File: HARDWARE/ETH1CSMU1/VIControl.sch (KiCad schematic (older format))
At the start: 102 parts

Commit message: Added ADC
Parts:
- added C406, C407, C408, C409, C410, C411, C412, C413, C414, C415, C416, C417, C418, C419, C420, C421, C422, C423: 100n, symbol Device:C
- D411, D412: renamed from D?; footprint Package_TO_SOT_SMD:SOT-23 -> (none)
- U402, U409: renamed from U?; footprint Package_SO:SOIC-8_3.9x4.9mm_P1.27mm -> (none)
- gave numbers to parts that had none: 78
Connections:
- net +15V: now also U401.8 (V+), U411.8 (V+), U412.8 (V+), U413.8 (V+), U415.8 (V+), U418.8 (V+), C407.1, C409.1, C411.1, C413.1, C415.1, C417.1, C419.1, C421.1, C423.1; no longer U401.8 (V+), U401.8 (V+), U403.8 (V+), U403.8 (V+), U407.8 (V+), U407.8 (V+)
- net +5V: now also U410.5 (VEE), U410.6 (GND); no longer U410.10 (VCC), U410.9 (VS)
- net +IDAC: now also U412.5 (+); no longer U412.5 (+)
- net -15V: now also U401.4 (V-), U411.4 (V-), U412.4 (V-), U413.4 (V-), U415.4 (V-), U418.4 (V-), C406.1, C408.1, C410.1, C412.1, C414.1, C416.1, C418.1, C420.1, C422.1; no longer U401.4 (V-), U401.4 (V-), U403.4 (V-), U403.4 (V-), U407.4 (V-), U407.4 (V-)
- net -IDAC: now also U412.3 (+); no longer U412.3 (+)
- net CurrentBoostIN: now also U415.7; no longer U415.7
- net GND: now also U401.3 (+), U410.10 (VCC), U410.9 (VS), U411.3 (+), U415.3 (+), U415.5 (+), C406.2, C407.2, C408.2, C409.2, C410.2, C411.2, C412.2, C413.2, C414.2, C415.2, C416.2, C417.2, C418.2, C419.2, C420.2, C421.2, C422.2, C423.2; no longer U401.3 (+), U410.5 (VEE), U410.6 (GND), U411.3 (+), U415.3 (+), U415.5 (+)
- net VI_CLAMP: now also U407.6 (-), U407.7; no longer U415.6 (-), U415.7
- net at U406.11 (VOUTB): now also U401.5 (+); no longer U411.5 (+)
- net at U406.5 (VOUTC): now also U411.5 (+); no longer U411.5 (+)
- net at R411.1, R415.2: now also U411.1; no longer U401.1
- net at R408.1, R411.2: now also U411.2 (-); no longer U401.2 (-)
- net at R412.1, R416.2: now also U411.7; no longer U411.7
- net at R406.1, R412.2: now also U411.6 (-); no longer U411.6 (-)
- net at R413.1, R417.2: now also U401.1; no longer U411.1
- net at R409.1, R413.2: now also U401.2 (-); no longer U411.2 (-)
- net at R414.1, R418.2: now also U401.7; no longer U411.7
- net at R407.1, R414.2: now also U401.6 (-); no longer U411.6 (-)
- net at D403.2 (A), R421.2: now also U412.2 (-); no longer U412.2 (-)
- net at D403.1 (K), D407.2 (A): now also U412.1; no longer U412.1
- net at D404.1 (K), R422.2: now also U412.6 (-); no longer U412.6 (-)
- net at D404.2 (A), D408.1 (K): now also U412.7; no longer U412.7
- net at D409.1 (K), D410.2 (A), R426.1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: now also U407.5 (+); no longer U415.5 (+)
- net at C404.1, D401.2 (A), D402.1 (K)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: now also U407.2 (-); no longer U412.2 (-)
- net at C404.2, D401.1 (K), D402.2 (A)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: now also U407.1; no longer U412.1
- net at R410.1: now also U407.3 (+); no longer U412.3 (+)
- net at C405.2, R428.1, R431.2: now also U415.2 (-); no longer U415.2 (-)
- net at C405.1, R431.1, R434.2: now also U415.1; no longer U415.1
- net at R434.1, R435.2: now also U415.6 (-); no longer U415.6 (-)
- net at R436.2, U418.1: now also U410.3 (-); no longer U410.2 (-)
- net at R446.2, R447.2: now also U403.3 (+); no longer U418.5 (+)
- net at R438.1, R445.2: now also U403.2 (-); no longer U418.6 (-)
- net at R437.1, R442.2: now also U418.6 (-); no longer U418.2 (-)
- net at R443.2, R444.2: now also U418.5 (+); no longer U418.3 (+)
- net at R419.2, R420.1: now also U403.5 (+); no longer U413.5 (+)
- net at D412.1: now also U410.7; no longer U410.8
- net at D412.2: now also U410.8; no longer U410.7
- new net: R438.2, U403.1, U410.1 (+)
- new net: U403.6 (-), U403.7
- new net: R437.2, U410.2 (-), U410.4 (+), U418.7
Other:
- moved on the sheet: C405, R419, R420, R428, R431, R432, R434, R435, U403C, U407C, U409B, U412A

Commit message: Commit
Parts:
- C406, C407, C408, C409, C410, C411, C412, C413, C414, C415, C416, C417, C418, C419, C420, C421, C422, C423: footprint (none) -> SMD:C_0603_Symbol1
- R406, R407, R408, R409, R410, R415, R416, R417, R418, R419, R420, R421, R422, R423, R424, R425, R428, R431, R433, R434, R435, R439, R440, R442, R443, R445, R446: footprint (none) -> SMD:R_0603_Symbol1
- R429, R430, R432: footprint (none) -> SMD:R_0603_Symbol2
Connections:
- net VREF renamed VREF+2V5
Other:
- moved on the sheet: D411, D412, R427, R429, R430, R433, R436, R437, R438, R439, R440, R441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

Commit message: Footprints
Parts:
- removed R432: 0, SMD:R_0603_Symbol2, symbol Device:R
- added C405, C406, C407, C408, C409, C410, C411, C412, C413, C414, C415, C435, C436: 100n, SMD:C_0603_Symbol1, symbol Device:C
- added U416: DG419xY, symbol Analog_Switch:DG419xY
- added U418: SN74LVC1T45, symbol logic_local:SN74LVC1T45
- C420: renamed from C405; footprint (none) -> SMD:C_0603_Symbol5
- D401, D402, D403, D404, D405, D406, D407, D408, D409, D410: value D_Schottky -> BAT54-02V
- renumbered C406 to C416, C407 to C417, C408 to C418, C409 to C419, C410 to C421, C411 to C422, C412 to C423, C413 to C424, C414 to C425, C415 to C426, C416 to C427, C417 to C428, C418 to C429, C419 to C430, C420 to C431, C421 to C432, C422 to C433, C423 to C434, R419 to R415, R420 to R416, R415 to R417, R416 to R418, R417 to R419, R418 to R420, R429 to R428, R428 to R429, R433 to R432, R434 to R433, R435 to R434, R436 to R435, R437 to R436, R438 to R437, R439 to R438, R440 to R439, R441 to R440, R442 to R441, R443 to R442, R444 to R443, R445 to R444, R446 to R445, R447 to R446, U411 to U402, U402 to U403, U418 to U404, U404 to U405, U405 to U406, U413 to U407, U403 to U408, U406 to U409, U415 to U410, U412 to U411, U408 to U412, U407 to U413, U409 to U414, U410 to U415, U414 to U417, U416 to U419, U417 to U420
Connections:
- net +15V: now also C436.1, U416.5 (VL)
- net +3V3: now also C406.1, C408.1, C410.1, C412.1, C414.1, U418.1 (VCCA)
- net +5V: now also C405.1, C407.1, C409.1, C411.1, C413.1, C415.1, U416.4 (V+), U418.6 (VCCB)
- net -15V: now also C435.1, U416.3 (GND)
- net CurrentBoostIN: now also U416.1; no longer R434.1, U410.7
- net GND: now also C405.2, C406.2, C407.2, C408.2, C409.2, C410.2, C411.2, C412.2, C413.2, C414.2, C415.2, C435.2, C436.2, U416.7 (V-), U418.2 (GND), U418.5 (DIR)
- net SIGN_SELECT: now also U418.3 (A)
- net VI_CLAMP: now also U416.8
- new net: R434.1, U410.7, U416.2
- new net: U416.6, U418.4 (B)
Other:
- moved on the sheet: C416, C417, C418, C419, C421, C422, C423, C424, C425, C426, C427, C428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

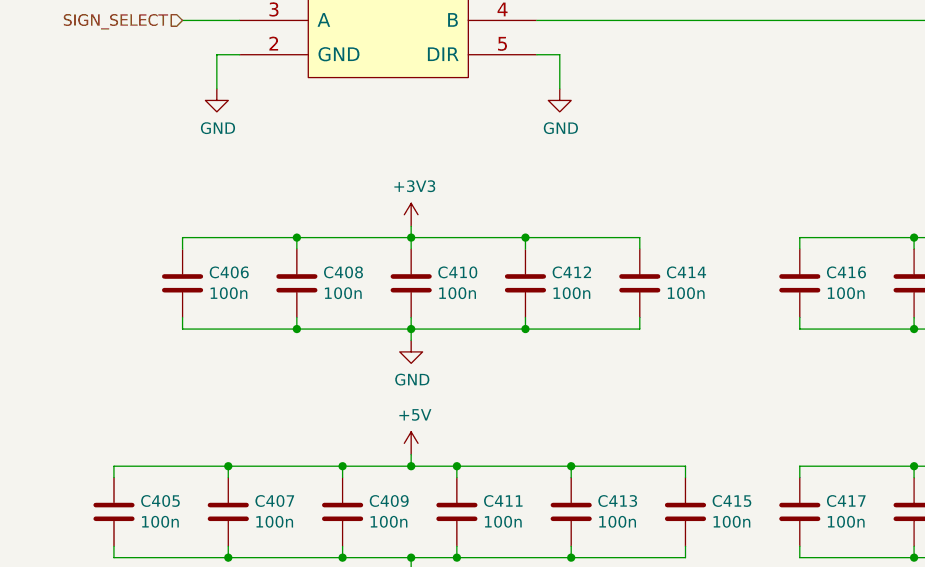
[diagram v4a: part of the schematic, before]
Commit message: Footprint selection
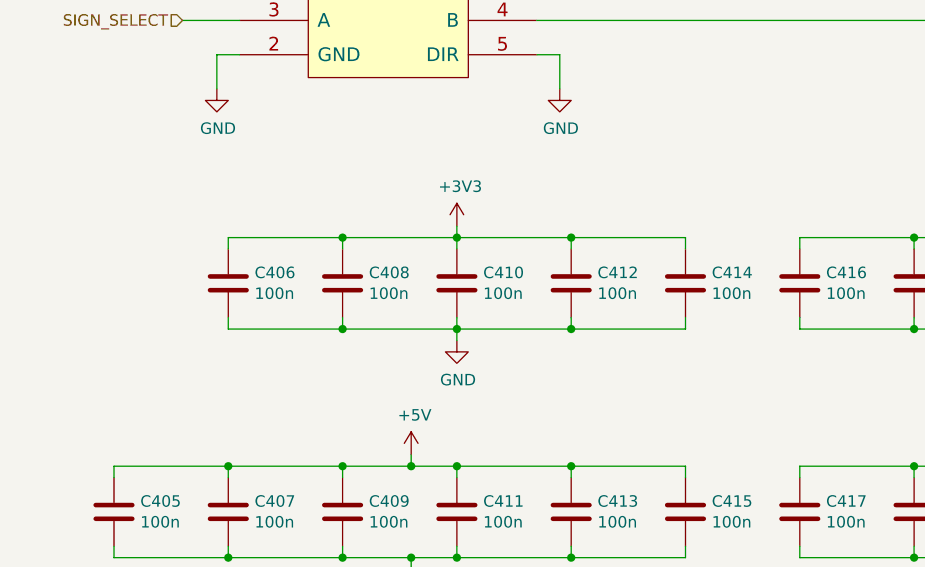
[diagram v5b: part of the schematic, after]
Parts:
- D401, D402, D403, D404, D405, D406, D407, D408, D409, D410: footprint (none) -> Diodes_SMD:D_SOD-523
- R401, R402: footprint (none) -> SMD:R_0603_Symbol2
- R403, R404: footprint (none) -> Resistors_SMD:R_0603
- R412, R414: footprint (none) -> SMD:R_0603_Symbol7
- R435, R436, R437, R440, R443, R446: footprint (none) -> SMD:R_0603_Symbol5
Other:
- moved on the sheet: C406, C408, C410, C412, C414
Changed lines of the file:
@@
 F 0 "R412" V 5493 2350 50  0000 C CNN
 F 1 "30k" V 5584 2350 50  0000 C CNN
-F 2 "" V 5630 2350 50  0001 C CNN
+F 2 "SMD:R_0603_Symbol7" V 5630 2350 50  0001 C CNN
 F 3 "~" H 5700 2350 50  0001 C CNN
 	1    5700 2350
@@
 F 0 "R414" V 5493 4800 50  0000 C CNN
 F 1 "30k" V 5584 4800 50  0000 C CNN
-F 2 "" V 5630 4800 50  0001 C CNN
+F 2 "SMD:R_0603_Symbol7" V 5630 4800 50  0001 C CNN
 F 3 "~" H 5700 4800 50  0001 C CNN
 	1    5700 4800
@@
 F 0 "D403" V 8146 1221 50  0000 R CNN
 F 1 "BAT54-02V" V 8055 1221 50  0000 R CNN
-F 2 "" H 8100 1300 50  0001 C CNN
+F 2 "Diodes_SMD:D_SOD-523" H 8100 1300 50  0001 C CNN
 F 3 "~" H 8100 1300 50  0001 C CNN
 	1    8100 1300
@@
 F 0 "D407" H 8300 1600 50  0000 C CNN
 F 1 "BAT54-02V" H 8300 1700 50  0000 C CNN
-F 2 "" H 8300 1500 50  0001 C CNN
+F 2 "Diodes_SMD:D_SOD-523" H 8300 1500 50  0001 C CNN
 F 3 "~" H 8300 1500 50  0001 C CNN
 	1    8300 1500
@@
 F 0 "D404" V 8054 2629 50  0000 L CNN
 F 1 "BAT54-02V" V 8145 2629 50  0000 L CNN
-F 2 "" H 8100 2550 50  0001 C CNN
+F 2 "Diodes_SMD:D_SOD-523" H 8100 2550 50  0001 C CNN
 F 3 "~" H 8100 2550 50  0001 C CNN
 	1    8100 2550
@@
 F 0 "D408" H 8300 2650 50  0000 C CNN
 F 1 "BAT54-02V" H 8300 2550 50  0000 C CNN
-F 2 "" H 8300 2750 50  0001 C CNN
+F 2 "Diodes_SMD:D_SOD-523" H 8300 2750 50  0001 C CNN
 F 3 "~" H 8300 2750 50  0001 C CNN
 	1    8300 2750
@@
 F 0 "D405" V 8146 3671 50  0000 R CNN
 F 1 "BAT54-02V" V 8055 3671 50  0000 R CNN
-F 2 "" H 8100 3750 50  0001 C CNN
+F 2 "Diodes_SMD:D_SOD-523" H 8100 3750 50  0001 C CNN
 F 3 "~" H 8100 3750 50  0001 C CNN
 	1    8100 3750
@@
 F 0 "D409" H 8300 4050 50  0000 C CNN
 F 1 "BAT54-02V" H 8300 4150 50  0000 C CNN
-F 2 "" H 8300 3950 50  0001 C CNN
+F 2 "Diodes_SMD:D_SOD-523" H 8300 3950 50  0001 C CNN
 F 3 "~" H 8300 3950 50  0001 C CNN
 	1    8300 3950
@@
 F 0 "D406" V 8054 5079 50  0000 L CNN
 F 1 "BAT54-02V" V 8145 5079 50  0000 L CNN
-F 2 "" H 8100 5000 50  0001 C CNN
+F 2 "Diodes_SMD:D_SOD-523" H 8100 5000 50  0001 C CNN
 F 3 "~" H 8100 5000 50  0001 C CNN
 	1    8100 5000
@@
 F 0 "D410" H 8300 5100 50  0000 C CNN
 F 1 "BAT54-02V" H 8300 5000 50  0000 C CNN
-F 2 "" H 8300 5200 50  0001 C CNN
+F 2 "Diodes_SMD:D_SOD-523" H 8300 5200 50  0001 C CNN
 F 3 "~" H 8300 5200 50  0001 C CNN
 	1    8300 5200
@@
 F 0 "D401" V 7346 6271 50  0000 R CNN
 F 1 "BAT54-02V" V 7255 6271 50  0000 R CNN
-F 2 "" H 7300 6350 50  0001 C CNN
+F 2 "Diodes_SMD:D_SOD-523" H 7300 6350 50  0001 C CNN
 F 3 "~" H 7300 6350 50  0001 C CNN
 	1    7300 6350
@@
 F 0 "D402" V 7854 6429 50  0000 L CNN
 F 1 "BAT54-02V" V 7945 6429 50  0000 L CNN
-F 2 "" H 7900 6350 50  0001 C CNN
+F 2 "Diodes_SMD:D_SOD-523" H 7900 6350 50  0001 C CNN
 F 3 "~" H 7900 6350 50  0001 C CNN
 	1    7900 6350
@@
 F 0 "R404" H 3620 7746 50  0000 L CNN
 F 1 "75k" H 3620 7655 50  0000 L CNN
-F 2 "" V 3480 7700 50  0001 C CNN
+F 2 "Resistors_SMD:R_0603" V 3480 7700 50  0001 C CNN
 F 3 "~" H 3550 7700 50  0001 C CNN
 	1    3550 7700
@@
 F 0 "R403" V 3093 7500 50  0000 C CNN
 F 1 "12k4" V 3184 7500 50  0000 C CNN
-F 2 "" V 3230 7500 50  0001 C CNN
+F 2 "Resistors_SMD:R_0603" V 3230 7500 50  0001 C CNN
 F 3 "~" H 3300 7500 50  0001 C CNN
 	1    3300 7500
@@
 F 0 "R402" H 2480 3904 50  0000 R CNN
 F 1 "0" H 2480 3995 50  0000 R CNN
-F 2 "" V 2480 3950 50  0001 C CNN
+F 2 "SMD:R_0603_Symbol2" V 2480 3950 50  0001 C CNN
 F 3 "~" H 2550 3950 50  0001 C CNN
 	1    2550 3950
@@
 F 0 "R401" H 2130 3904 50  0000 R CNN
 F 1 "0" H 2130 3995 50  0000 R CNN
-F 2 "" V 2130 3950 50  0001 C CNN
+F 2 "SMD:R_0603_Symbol2" V 2130 3950 50  0001 C CNN
 F 3 "~" H 2200 3950 50  0001 C CNN
 	1    2200 3950
@@
 F 0 "R435" V 14343 800 50  0000 C CNN
 F 1 "2k49" V 14434 800 50  0000 C CNN
-F 2 "" V 14480 800 50  0001 C CNN
+F 2 "SMD:R_0603_Symbol5" V 14480 800 50  0001 C CNN
 F 3 "~" H 14550 800 50  0001 C CNN
 	1    14550 800
@@
 F 0 "R440" V 14993 1700 50  0000 C CNN
 F 1 "2k49" V 15084 1700 50  0000 C CNN
-F 2 "" V 15130 1700 50  0001 C CNN
+F 2 "SMD:R_0603_Symbol5" V 15130 1700 50  0001 C CNN
 F 3 "~" H 15200 1700 50  0001 C CNN
 	1    15200 1700
@@
 F 0 "R437" V 14343 3500 50  0000 C CNN
 F 1 "2k49" V 14434 3500 50  0000 C CNN
-F 2 "" V 14480 3500 50  0001 C CNN
+F 2 "SMD:R_0603_Symbol5" V 14480 3500 50  0001 C CNN
 F 3 "~" H 14550 3500 50  0001 C CNN
 	1    14550 3500
@@
 F 0 "R446" V 14993 4400 50  0000 C CNN
 F 1 "2k49" V 15084 4400 50  0000 C CNN
-F 2 "" V 15130 4400 50  0001 C CNN
+F 2 "SMD:R_0603_Symbol5" V 15130 4400 50  0001 C CNN
 F 3 "~" H 15200 4400 50  0001 C CNN
 	1    15200 4400
@@
 F 0 "R436" V 14343 2150 50  0000 C CNN
 F 1 "2k49" V 14434 2150 50  0000 C CNN
-F 2 "" V 14480 2150 50  0001 C CNN
+F 2 "SMD:R_0603_Symbol5" V 14480 2150 50  0001 C CNN
 F 3 "~" H 14550 2150 50  0001 C CNN
 	1    14550 2150
@@
 F 0 "R443" V 14993 3050 50  0000 C CNN
 F 1 "2k49" V 15084 3050 50  0000 C CNN
-F 2 "" V 15130 3050 50  0001 C CNN
+F 2 "SMD:R_0603_Symbol5" V 15130 3050 50  0001 C CNN
 F 3 "~" H 15200 3050 50  0001 C CNN
 	1    15200 3050
@@
 L Device:C C406
 U 1 1 5C341DFF
-P 8400 8450
-F 0 "C406" H 8515 8496 50  0000 L CNN
-F 1 "100n" H 8515 8405 50  0000 L CNN
-F 2 "SMD:C_0603_Symbol1" H 8438 8300 50  0001 C CNN
-F 3 "~" H 8400 8450 50  0001 C CNN
-	1    8400 8450
+P 8600 8450
+F 0 "C406" H 8715 8496 50  0000 L CNN
+F 1 "100n" H 8715 8405 50  0000 L CNN
+F 2 "SMD:C_0603_Symbol1" H 8638 8300 50  0001 C CNN
+F 3 "~" H 8600 8450 50  0001 C CNN
+	1    8600 8450
 	1    0    0    -1
 $EndComp
@@
 L Device:C C408
 U 1 1 5C341E05
-P 8900 8450
-F 0 "C408" H 9015 8496 50  0000 L CNN
-F 1 "100n" H 9015 8405 50  0000 L CNN
-F 2 "SMD:C_0603_Symbol1" H 8938 8300 50  0001 C CNN
-F 3 "~" H 8900 8450 50  0001 C CNN
-	1    8900 8450
+P 9100 8450
+F 0 "C408" H 9215 8496 50  0000 L CNN
+F 1 "100n" H 9215 8405 50  0000 L CNN
+F 2 "SMD:C_0603_Symbol1" H 9138 8300 50  0001 C CNN
+F 3 "~" H 9100 8450 50  0001 C CNN
+	1    9100 8450
 	1    0    0    -1
 $EndComp
@@
 L Device:C C410
 U 1 1 5C341E0B
-P 9400 8450
-F 0 "C410" H 9515 8496 50  0000 L CNN
-F 1 "100n" H 9515 8405 50  0000 L CNN
-F 2 "SMD:C_0603_Symbol1" H 9438 8300 50  0001 C CNN
-F 3 "~" H 9400 8450 50  0001 C CNN
-	1    9400 8450
+P 9600 8450
+F 0 "C410" H 9715 8496 50  0000 L CNN
+F 1 "100n" H 9715 8405 50  0000 L CNN
+F 2 "SMD:C_0603_Symbol1" H 9638 8300 50  0001 C CNN
+F 3 "~" H 9600 8450 50  0001 C CNN
+	1    9600 8450
 	1    0    0    -1
 $EndComp
@@
 L Device:C C412
 U 1 1 5C341E11
-P 9900 8450
-F 0 "C412" H 10015 8496 50  0000 L CNN
-F 1 "100n" H 10015 8405 50  0000 L CNN
-F 2 "SMD:C_0603_Symbol1" H 9938 8300 50  0001 C CNN
-F 3 "~" H 9900 8450 50  0001 C CNN
-	1    9900 8450
+P 10100 8450
+F 0 "C412" H 10215 8496 50  0000 L CNN
+F 1 "100n" H 10215 8405 50  0000 L CNN
+F 2 "SMD:C_0603_Symbol1" H 10138 8300 50  0001 C CNN
+F 3 "~" H 10100 8450 50  0001 C CNN
+	1    10100 8450
 	1    0    0    -1
 $EndComp
@@
 L Device:C C414
 U 1 1 5C341E17
-P 10400 8450
-F 0 "C414" H 10515 8496 50  0000 L CNN
-F 1 "100n" H 10515 8405 50  0000 L CNN
-F 2 "SMD:C_0603_Symbol1" H 10438 8300 50  0001 C CNN
-F 3 "~" H 10400 8450 50  0001 C CNN
-	1    10400 8450
+P 10600 8450
+F 0 "C414" H 10715 8496 50  0000 L CNN
+F 1 "100n" H 10715 8405 50  0000 L CNN
+F 2 "SMD:C_0603_Symbol1" H 10638 8300 50  0001 C CNN
+F 3 "~" H 10600 8450 50  0001 C CNN
+	1    10600 8450
 	1    0    0    -1
 $EndComp
 Wire Wire Line
-	8400 8300 8400 8250
+	8600 8300 8600 8250
 Wire Wire Line
-	8400 8250 8900 8250
+	8600 8250 9100 8250
 Wire Wire Line
-	10400 8300 10400 8250
+	10600 8300 10600 8250
 Wire Wire Line
-	9900 8300 9900 8250
-Connection ~ 9900 8250
+	10100 8300 10100 8250
+Connection ~ 10100 8250
 Wire Wire Line
-	9900 8250 10400 8250
+	10100 8250 10600 8250
 Wire Wire Line
-	9400 8300 9400 8250
-Connection ~ 9400 8250
+	9600 8300 9600 8250
+Connection ~ 9600 8250
 Wire Wire Line
-	9400 8250 9900 8250
+	9600 8250 10100 8250
 Wire Wire Line
-	8900 8300 8900 8250
-Connection ~ 8900 8250
+	9100 8300 9100 8250
+Connection ~ 9100 8250
 Wire Wire Line
-	8900 8250 9400 8250
+	9100 8250 9600 8250
 Wire Wire Line
-	8400 8600 8400 8650
+	8600 8600 8600 8650
 Wire Wire Line
-	8400 8650 8900 8650
+	8600 8650 9100 8650
 Wire Wire Line
-	10400 8600 10400 8650
+	10600 8600 10600 8650
 Wire Wire Line
-	9900 8600 9900 8650
-Connection ~ 9900 8650
+	10100 8600 10100 8650
+Connection ~ 10100 8650
 Wire Wire Line
-	9900 8650 10400 8650
+	10100 8650 10600 8650
 Wire Wire Line
-	9400 8600 9400 8650
-Connection ~ 9400 8650
+	9600 8600 9600 8650
+Connection ~ 9600 8650
 Wire Wire Line
-	9400 8650 9900 8650
+	9600 8650 10100 8650
 Wire Wire Line
-	8900 8600 8900 8650
-Connection ~ 8900 8650
+	9100 8600 9100 8650
+Connection ~ 9100 8650
 Wire Wire Line
-	8900 8650 9400 8650
+	9100 8650 9600 8650
 $Comp
 L power:GND #PWR0461
 U 1 1 5C49DEA2
-P 9400 8700
-F 0 "#PWR0461" H 9400 8450 50  0001 C CNN
-F 1 "GND" H 9405 8527 50  0000 C CNN
-F 2 "" H 9400 8700 50  0001 C CNN
-F 3 "" H 9400 8700 50  0001 C CNN
-	1    9400 8700
+P 9600 8700
+F 0 "#PWR0461" H 9600 8450 50  0001 C CNN
+F 1 "GND" H 9605 8527 50  0000 C CNN
+F 2 "" H 9600 8700 50  0001 C CNN
+F 3 "" H 9600 8700 50  0001 C CNN
+	1    9600 8700
 	1    0    0    -1
 $EndComp
 Wire Wire Line
-	9400 8700 9400 8650
+	9600 8700 9600 8650
 $Comp
 L power:+3V3 #PWR0460
 U 1 1 5C4CBE36
-P 9400 8200
-F 0 "#PWR0460" H 9400 8050 50  0001 C CNN
-F 1 "+3V3" H 9415 8373 50  0000 C CNN
-F 2 "" H 9400 8200 50  0001 C CNN
-F 3 "" H 9400 8200 50  0001 C CNN
-	1    9400 8200
+P 9600 8200
+F 0 "#PWR0460" H 9600 8050 50  0001 C CNN
+F 1 "+3V3" H 9615 8373 50  0000 C CNN
+F 2 "" H 9600 8200 50  0001 C CNN
+F 3 "" H 9600 8200 50  0001 C CNN
+	1    9600 8200
 	1    0    0    -1
 $EndComp
 Wire Wire Line
-	9400 8200 9400 8250
+	9600 8200 9600 8250
 $Comp
 L Device:C C407

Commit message: Redesigned feedback circuit.
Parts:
- removed U409: DAC80004, symbol DAC_local:DAC80004
- added U409: DAC80004, Housings_SSOP:TSSOP-14_4.4x5mm_Pitch0.65mm, symbol DAC_local:DAC80004_TSSOP
- U401, U402, U403, U404, U407, U408, U410, U411, U412, U413: footprint (none) -> Housings_SOIC:SOIC-8_3.9x4.9mm_Pitch1.27mm
- U405, U406, U418, U420: footprint (none) -> SMD:SC70-6
- U414, U416: value DG419xY -> DG419; footprint (none) -> Housings_SOIC:SOIC-8_3.9x4.9mm_Pitch1.27mm
- U415: footprint (none) -> Housings_SSOP:MSOP-10_3x3mm_Pitch0.5mm
- U417: footprint (none) -> SMD:AQY2
- U419: footprint (none) -> TO_SOT_Packages_SMD:SOT-23-5
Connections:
- net +3V3: now also U409.3 (VDD)
- net GND: now also U409.12 (GND)
- net QDAC_SCLK: now also U409.14 (SCLK)
- net QDAC_SDIN: now also U409.13 (SDIN)
- net QDAC_SDO: now also U409.8 (SDO)
- net QDAC_~CLR: now also U409.9 (~CLR)
- net QDAC_~LDAC: now also U409.1 (~LDAC)
- net QDAC_~SYNC: now also U409.2 (~SYNC)
- net VREF+2V5: now also U409.7 (REFIN)
- net at R409.2: now also U409.10 (VOUTD)
- net at U401.5 (+): now also U409.11 (VOUTB)
- net at R408.2: now also U409.4 (VOUTA)
- net at U402.5 (+): now also U409.5 (VOUTC)
- net at R401.2, R402.2: now also U409.6 (POR)

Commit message: Schematic development
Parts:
- renumbered C401 to C301, C402 to C302, C403 to C303, C404 to C304, C405 to C305, C406 to C306, C407 to C307, C408 to C308, C409 to C309, C410 to C310, C411 to C311, C412 to C312, C413 to C313, C414 to C314, C415 to C315, C416 to C316, C417 to C317, C418 to C318, C419 to C319, C420 to C320, C421 to C321, C422 to C322, C423 to C323, C424 to C324, C425 to C325, C426 to C326, C427 to C327, C428 to C328, C429 to C329, C430 to C330, C431 to C331, C432 to C332, C433 to C333, C434 to C334, C435 to C335, C436 to C336, D401 to D301, D402 to D302, D403 to D303, D404 to D304, D405 to D305, D406 to D306, D407 to D307, D408 to D308, D409 to D309, D410 to D310, D411 to D311, D412 to D312, R401 to R301, R402 to R302, R403 to R303, R404 to R304, R405 to R305, R406 to R306, R407 to R307, R408 to R308, R409 to R309, R410 to R310, R411 to R311, R412 to R312, R413 to R313, R414 to R314, R415 to R315, R416 to R316, R417 to R317, R418 to R318, R419 to R319, R420 to R320, R421 to R321, R422 to R322, R423 to R323, R424 to R324, R425 to R325, R426 to R326, R427 to R327, R428 to R328, R429 to R329, R430 to R330, R431 to R331, R432 to R332, R433 to R333, R434 to R334, R435 to R335, R436 to R336, R437 to R337, R438 to R338, R439 to R339, R440 to R340, R441 to R341, R442 to R342, R443 to R343, R444 to R344, R445 to R345, R446 to R346, U401 to U301, U402 to U302, U403 to U303, U404 to U304, U405 to U305, U406 to U306, U407 to U307, U408 to U308, U409 to U309, U410 to U310, U411 to U311, U412 to U312, U413 to U313, U414 to U314, U415 to U315, U416 to U316, U417 to U317, U418 to U318, U419 to U319, U420 to U320
